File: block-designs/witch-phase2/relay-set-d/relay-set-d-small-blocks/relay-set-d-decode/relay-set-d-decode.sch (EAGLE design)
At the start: 85 parts, among them IC1 74LS138D, IC10 74LVC1G32DBV, IC11 74LVC1G32DBV, IC12 74LVC1G32DBV, IC13 74LVC1G125DBV, IC14 74LVC1G125DBV, IC15 74LVC1G125DBV, IC16 74LVC1G125DBV, IC17 74LVC1G125DBV, IC18 74LVC1G125DBV, IC19 74LVC1G125DBV, IC2 74LS138D, IC20 74LVC1G125DBV, IC21 74LVC1G125DBV, IC22 74LVC1G125DBV, IC23 74LVC1G125DBV, IC24 74LVC1G125DBV, IC25 74LVC1G04DBV, IC26 74LVC1G04DBV, IC3 74LS138D, IC4 74LS138D, IC5 74LVC1G32DBV, IC6 74LVC1G32DBV, IC7 74LVC1G32DBV, IC8 74LVC1G32DBV, IC9 74LVC1G32DBV

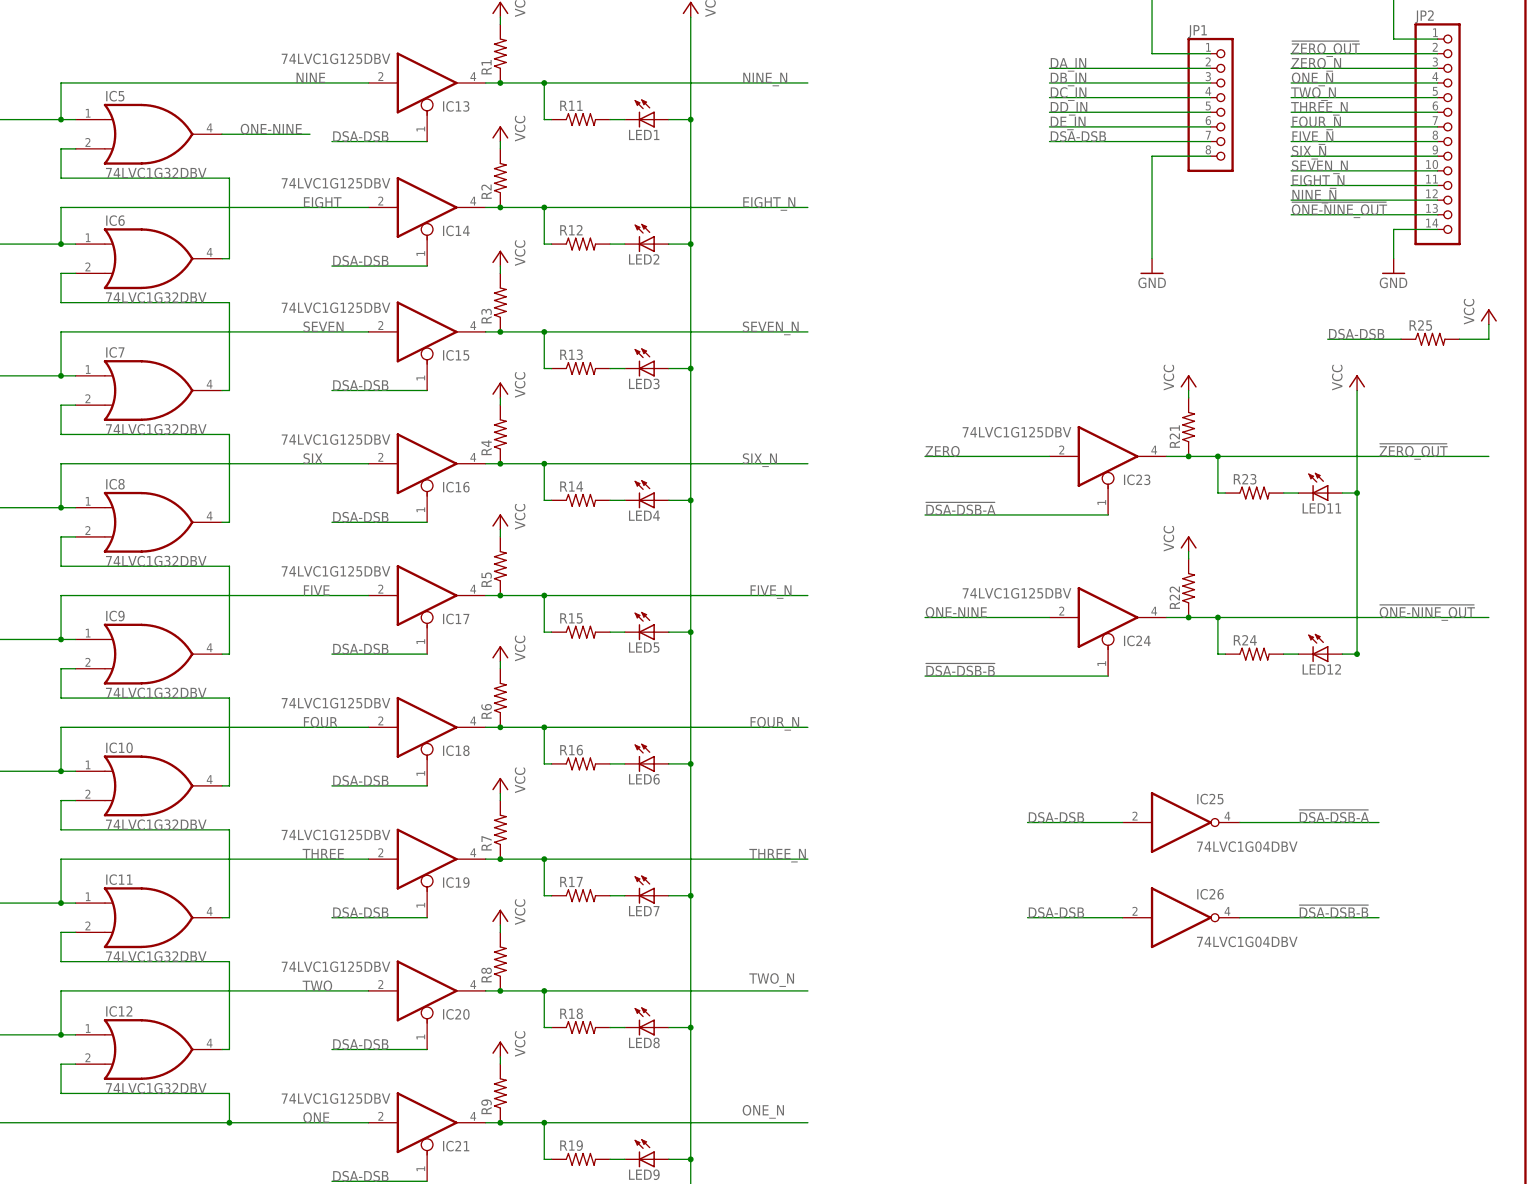
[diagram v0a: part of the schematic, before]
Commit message: fixes for the decode - change OR gates to AND gates
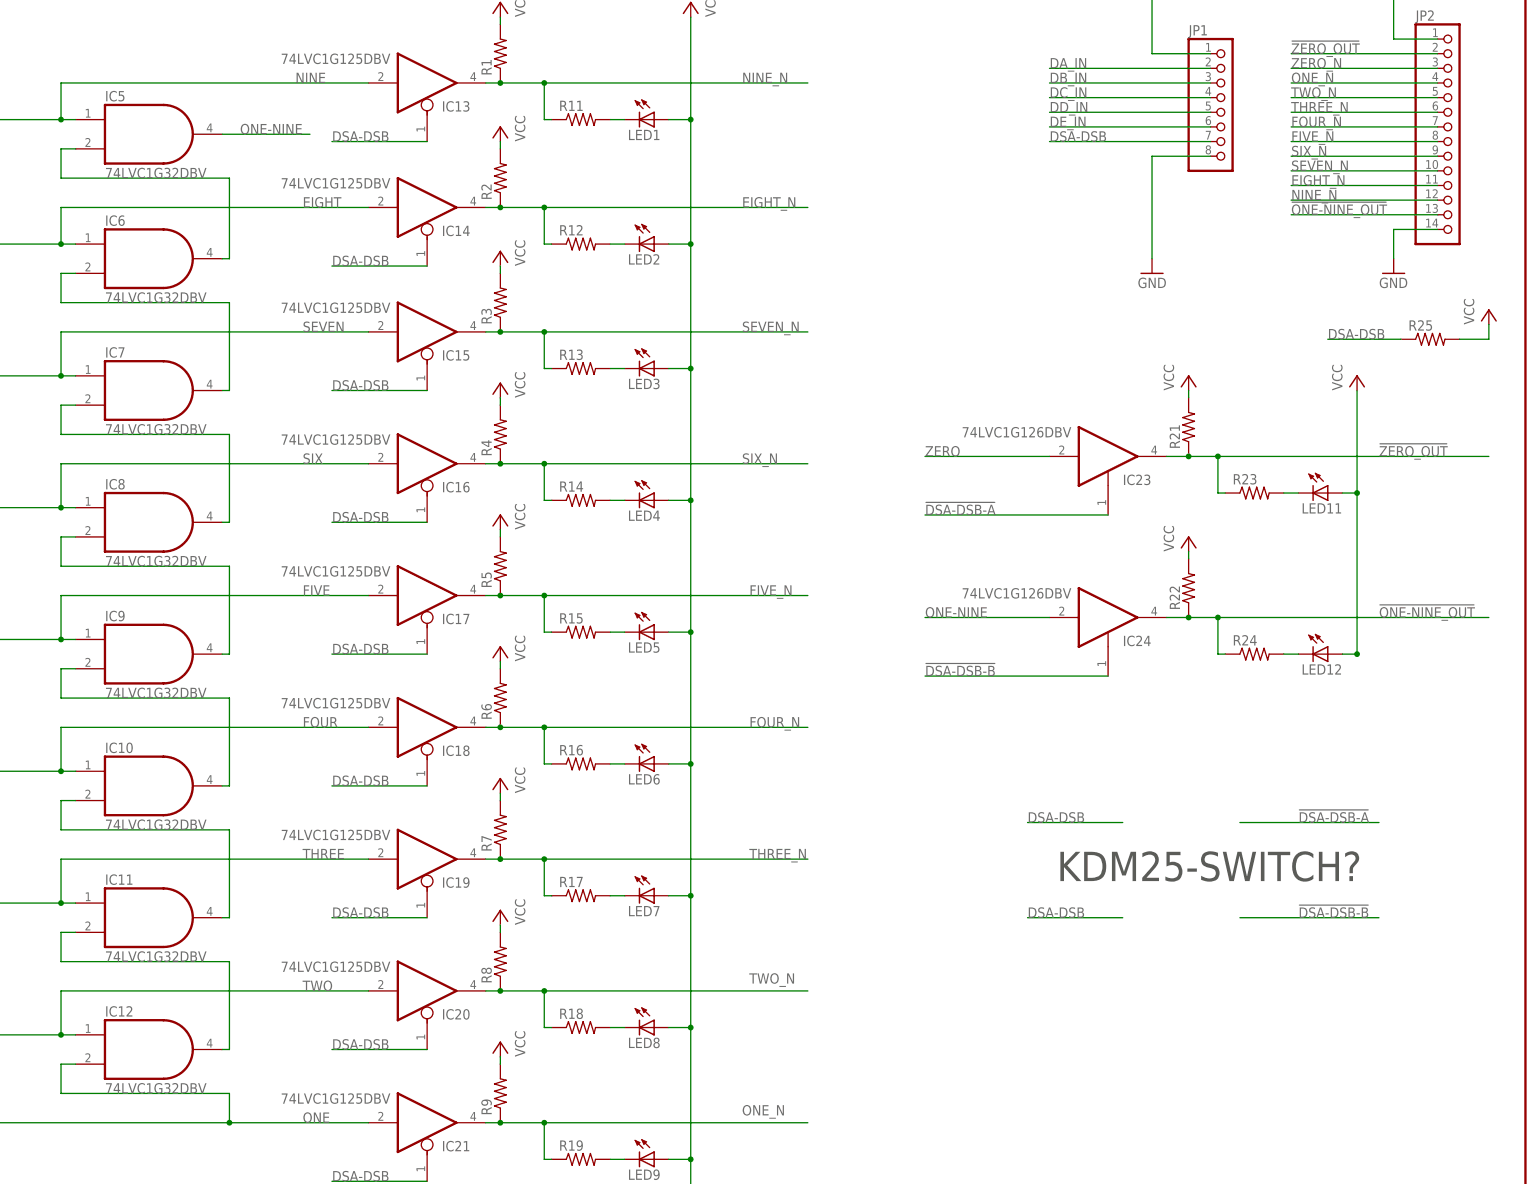
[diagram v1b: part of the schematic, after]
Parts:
- removed IC25, IC26: 74LVC1G04DBV, 74xx-little-us:74LVC1G04DBV
- IC10, IC11, IC12, IC5, IC6, IC7, IC8, IC9: device 74xx-little-us:74AHC1G32DBV -> 74xx-little-us:74LVC1G08DBV
- IC23, IC24: value 74LVC1G125DBV -> 74LVC1G126DBV; device 74xx-little-us:74LVC1G125DBV -> 74xx-little-us:74LVC1G126DBV
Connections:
- net !DSA-DSB-A: no longer IC25A.O
- net !DSA-DSB-B: no longer IC26A.O
- net DSA-DSB: no longer IC25A.I, IC26A.I
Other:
- note added: "KDM25-SWITCH?"
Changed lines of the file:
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@@
 </classes>
 <parts>
-<part name="IC12" library="74xx-little-us" deviceset="74*1G32" device="DBV" technology="AHC" value="74LVC1G32DBV"/>
-<part name="IC11" library="74xx-little-us" deviceset="74*1G32" device="DBV" technology="AHC" value="74LVC1G32DBV"/>
-<part name="IC10" library="74xx-little-us" deviceset="74*1G32" device="DBV" technology="AHC" value="74LVC1G32DBV"/>
-<part name="IC9" library="74xx-little-us" deviceset="74*1G32" device="DBV" technology="AHC" value="74LVC1G32DBV"/>
-<part name="IC8" library="74xx-little-us" deviceset="74*1G32" device="DBV" technology="AHC" value="74LVC1G32DBV"/>
-<part name="IC7" library="74xx-little-us" deviceset="74*1G32" device="DBV" technology="AHC" value="74LVC1G32DBV"/>
-<part name="IC6" library="74xx-little-us" deviceset="74*1G32" device="DBV" technology="AHC" value="74LVC1G32DBV"/>
-<part name="IC5" library="74xx-little-us" deviceset="74*1G32" device="DBV" technology="AHC" value="74LVC1G32DBV"/>
+<part name="IC12" library="74xx-little-us" deviceset="74*1G08" device="DBV" technology="LVC" value="74LVC1G32DBV"/>
+<part name="IC11" library="74xx-little-us" deviceset="74*1G08" device="DBV" technology="LVC" value="74LVC1G32DBV"/>
+<part name="IC10" library="74xx-little-us" deviceset="74*1G08" device="DBV" technology="LVC" value="74LVC1G32DBV"/>
+<part name="IC9" library="74xx-little-us" deviceset="74*1G08" device="DBV" technology="LVC" value="74LVC1G32DBV"/>
+<part name="IC8" library="74xx-little-us" deviceset="74*1G08" device="DBV" technology="LVC" value="74LVC1G32DBV"/>
+<part name="IC7" library="74xx-little-us" deviceset="74*1G08" device="DBV" technology="LVC" value="74LVC1G32DBV"/>
+<part name="IC6" library="74xx-little-us" deviceset="74*1G08" device="DBV" technology="LVC" value="74LVC1G32DBV"/>
+<part name="IC5" library="74xx-little-us" deviceset="74*1G08" device="DBV" technology="LVC" value="74LVC1G32DBV"/>
 <part name="JP1" library="pinhead" deviceset="PINHD-1X8" device=""/>
 <part name="GND4" library="supply1" deviceset="GND" device=""/>
@@
 <part name="P+20" library="supply1" deviceset="VCC" device=""/>
 <part name="R1" library="resistor" deviceset="R-US_" device="R0805"/>
-<part name="IC24" library="74xx-little-us" deviceset="74*1G125" device="DBV" technology="LVC"/>
+<part name="IC24" library="74xx-little-us" deviceset="74*1G126" device="DBV" technology="LVC"/>
 <part name="IC13" library="74xx-little-us" deviceset="74*1G125" device="DBV" technology="LVC"/>
 <part name="IC14" library="74xx-little-us" deviceset="74*1G125" device="DBV" technology="LVC"/>
@@
 <part name="R9" library="resistor" deviceset="R-US_" device="R0805"/>
 <part name="R10" library="resistor" deviceset="R-US_" device="R0805"/>
-<part name="IC23" library="74xx-little-us" deviceset="74*1G125" device="DBV" technology="LVC"/>
+<part name="IC23" library="74xx-little-us" deviceset="74*1G126" device="DBV" technology="LVC"/>
 <part name="R21" library="resistor" deviceset="R-US_" device="R0805"/>
 <part name="R22" library="resistor" deviceset="R-US_" device="R0805"/>
-<part name="IC25" library="74xx-little-us" deviceset="74*1G04" device="DBV" technology="LVC"/>
 <part name="LED10" library="led" deviceset="LED" device="CHIP-LED0805"/>
 <part name="R20" library="resistor" deviceset="R-US_" device="R0805"/>
@@
 <part name="P+17" library="supply1" deviceset="VCC" device=""/>
 <part name="P+18" library="supply1" deviceset="VCC" device=""/>
-<part name="IC26" library="74xx-little-us" deviceset="74*1G04" device="DBV" technology="LVC"/>
 <part name="C5" library="resistor" deviceset="C-US" device="C0805"/>
 <part name="C7" library="resistor" deviceset="C-US" device="C0805"/>
@@
 <sheet>
 <plain>
+<text x="320.04" y="105.41" size="5.08" layer="97">KDM25-SWITCH?</text>
 </plain>
 <instances>
@@
 <instance part="R21" gate="G$1" x="342.9" y="184.15" rot="R90"/>
 <instance part="R22" gate="G$1" x="342.9" y="156.21" rot="R90"/>
-<instance part="IC25" gate="A" x="341.63" y="115.57"/>
 <instance part="LED10" gate="G$1" x="250.19" y="27.94" rot="R270"/>
 <instance part="R20" gate="G$1" x="237.49" y="27.94"/>
@@
 <instance part="P+17" gate="VCC" x="342.9" y="165.1"/>
 <instance part="P+18" gate="VCC" x="372.11" y="193.04"/>
-<instance part="IC26" gate="A" x="341.63" y="99.06"/>
 <instance part="C5" gate="G$1" x="33.02" y="100.33"/>
 <instance part="C7" gate="G$1" x="40.64" y="100.33"/>
@@
 </segment>
 <segment>
-<pinref part="IC25" gate="A" pin="I"/>
 <wire x1="331.47" y1="115.57" x2="314.96" y2="115.57" width="0.1524" layer="91"/>
 <label x="314.96" y="115.57" size="1.778" layer="95"/>
@@
 </segment>
 <segment>
-<pinref part="IC26" gate="A" pin="I"/>
 <wire x1="331.47" y1="99.06" x2="314.96" y2="99.06" width="0.1524" layer="91"/>
 <label x="314.96" y="99.06" size="1.778" layer="95"/>
@@
 </segment>
 <segment>
-<pinref part="IC25" gate="A" pin="O"/>
 <wire x1="351.79" y1="115.57" x2="375.92" y2="115.57" width="0.1524" layer="91"/>
 <label x="361.95" y="115.57" size="1.778" layer="95"/>
@@
 <net name="!DSA-DSB-B" class="0">
 <segment>
-<pinref part="IC26" gate="A" pin="O"/>
 <wire x1="351.79" y1="99.06" x2="375.92" y2="99.06" width="0.1524" layer="91"/>
 <label x="361.95" y="99.06" size="1.778" layer="95"/>

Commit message: remove 0 and 1-9 special decodes for basic testing
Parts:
- removed IC10, IC11, IC12, IC5, IC6, IC7, IC8, IC9: 74LVC1G32DBV, 74xx-little-us:74LVC1G08DBV
- removed IC23, IC24: 74LVC1G126DBV, 74xx-little-us:74LVC1G126DBV
- removed LED11, LED12: (no value), led:LEDCHIP-LED0805
- removed R21, R22, R23, R24: (no value), resistor:R-US_R0805
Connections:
- removed net !DSA-DSB-A: IC23A.OE
- removed net !DSA-DSB-B: IC24A.OE
- removed net N$11: IC8A.I1, IC9A.O
- removed net N$12: IC10A.O, IC9A.I1
- removed net N$13: IC10A.I1, IC11A.O
- removed net N$14: IC11A.I1, IC12A.O
- removed net N$15: LED11.C, R23.2
- removed net N$17: IC5A.I1, IC6A.O
- removed net N$18: IC6A.I1, IC7A.O
- removed net N$19: IC7A.I1, IC8A.O
- removed net N$20: LED12.C, R24.2
- removed net ONE-NINE: IC24A.I, IC5A.O
- net !ONE-NINE_OUT: no longer IC24A.O, R22.1, R24.1
- net !ZERO_OUT: no longer IC23A.O, R21.1, R23.1
- net EIGHT: no longer IC6A.I0
- net FIVE: no longer IC9A.I0
- net FOUR: no longer IC10A.I0
- net NINE: no longer IC5A.I0
- net ONE: no longer IC12A.I1
- net SEVEN: no longer IC7A.I0
- net SIX: no longer IC8A.I0
- net THREE: no longer IC11A.I0
- net TWO: no longer IC12A.I0
- net VCC: no longer LED11.A, LED12.A, R21.2, R22.2
- net ZERO: no longer IC23A.I
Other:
- note removed: "KDM25-SWITCH?"
- moved on the sheet: C1, C10, C11, C12, C13, C14, C15, C16, C17, C18, C19, C2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
